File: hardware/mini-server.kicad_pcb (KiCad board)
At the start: 6 copper layers, 1 part, among them U1 NT5CB256M16ER-FL

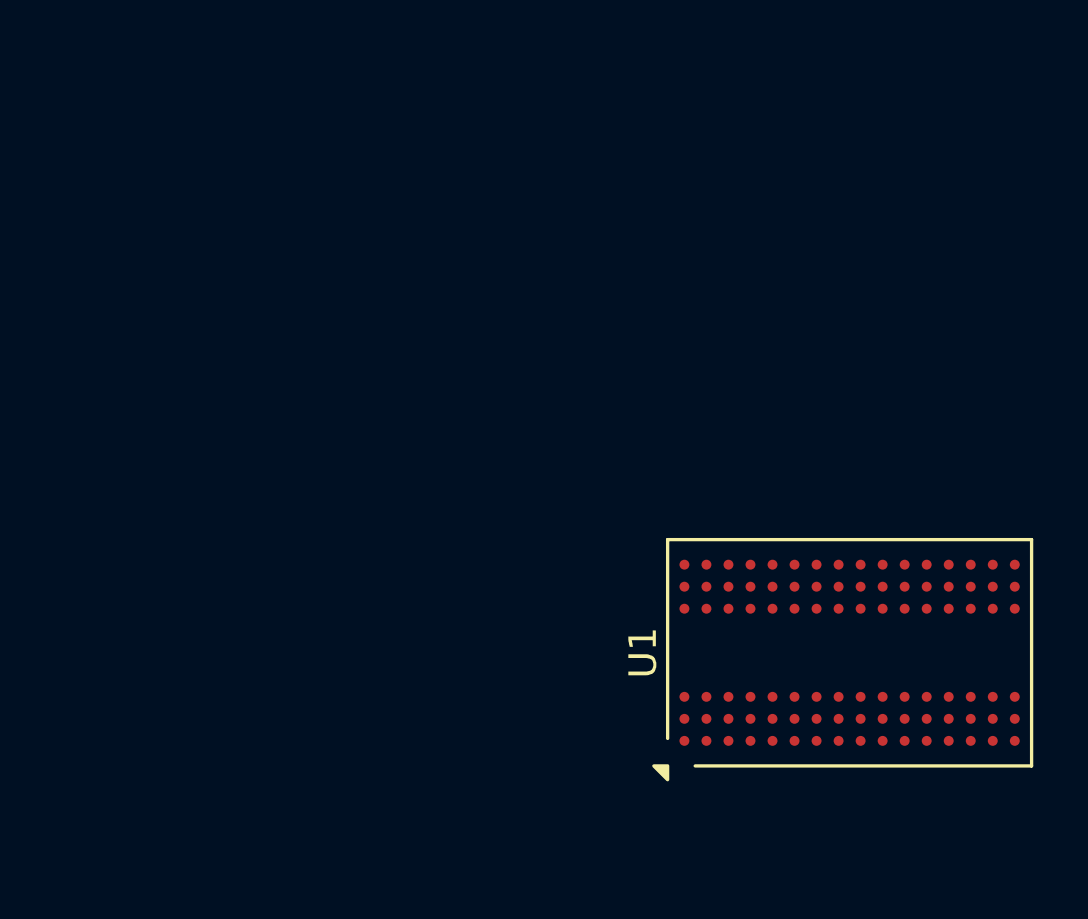
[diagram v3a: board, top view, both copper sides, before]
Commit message: Address and Control signals of DDR3 ram routed
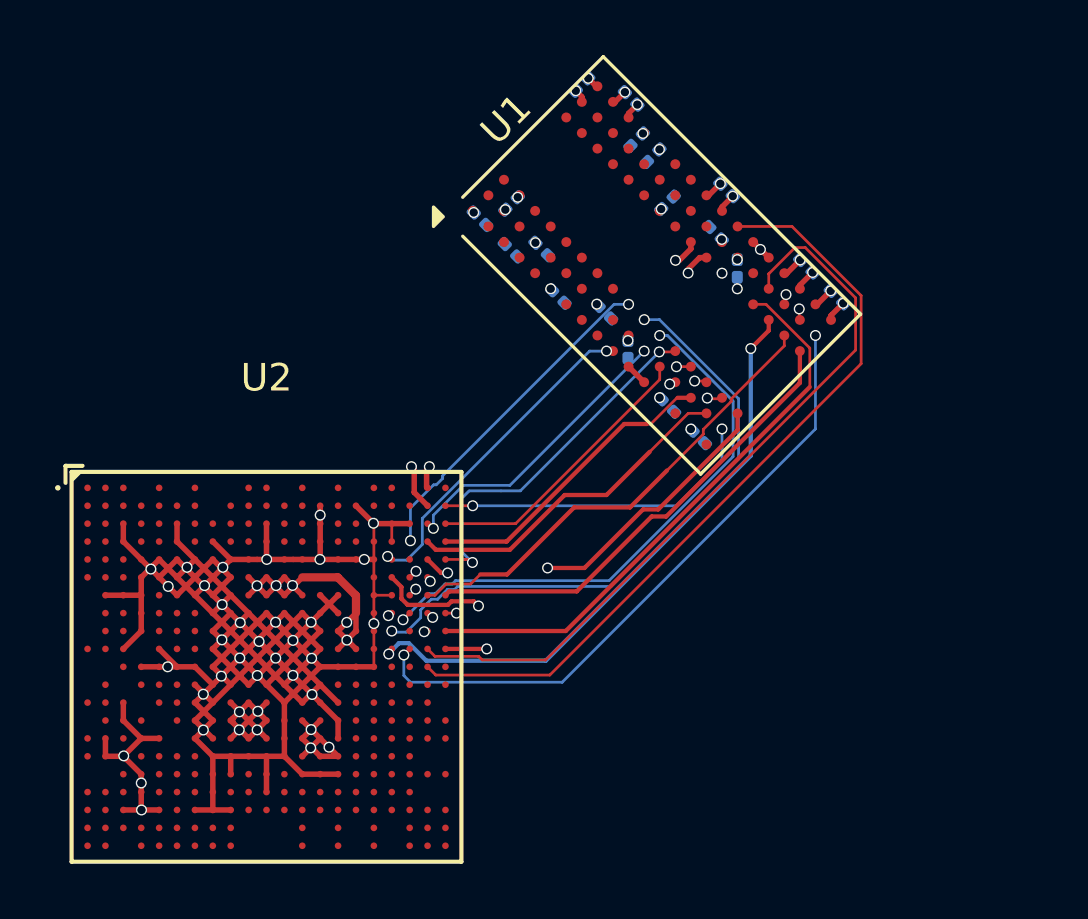
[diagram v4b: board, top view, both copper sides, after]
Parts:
- added C0: 100n, Capacitor_SMD:C_0201_0603Metric, B.Cu at (138.5, 74.4)
- added C1: 100n, Capacitor_SMD:C_0201_0603Metric, B.Cu at (137.4, 75.0)
- added C10: 100n, Capacitor_SMD:C_0201_0603Metric, B.Cu at (142.8, 70.6)
- added C11: 100n, Capacitor_SMD:C_0201_0603Metric, B.Cu at (143.0, 72.1)
- added C12: 100n, Capacitor_SMD:C_0201_0603Metric, B.Cu at (143.6, 72.7)
- added C13: 100n, Capacitor_SMD:C_0201_0603Metric, B.Cu at (146.3, 73.9)
- added C14: 100n, Capacitor_SMD:C_0201_0603Metric, B.Cu at (144.2, 74.4)
- added C15: 100n, Capacitor_SMD:C_0201_0603Metric, B.Cu at (145.9, 75.5)
- added C16: 100n, Capacitor_SMD:C_0201_0603Metric, B.Cu at (149.2, 76.7)
- added C17: 100n, Capacitor_SMD:C_0201_0603Metric, B.Cu at (150.3, 77.8)
- added C2: 100n, Capacitor_SMD:C_0201_0603Metric, B.Cu at (138.5, 76.1)
- added C3: 100n, Capacitor_SMD:C_0201_0603Metric, B.Cu at (140.2, 77.8)
- added C4: 100n, Capacitor_SMD:C_0201_0603Metric, B.Cu at (141.9, 78.4)
- added C5: 100n, Capacitor_SMD:C_0201_0603Metric, B.Cu at (142.7, 79.7)
- added C6: 100n, Capacitor_SMD:C_0201_0603Metric, B.Cu at (144.2, 81.8)
- added C7: 100n, Capacitor_SMD:C_0201_0603Metric, B.Cu at (145.3, 82.9)
- added C8: 100n, Capacitor_SMD:C_0201_0603Metric, B.Cu at (139.6, 76.1)
- added C9: 100n, Capacitor_SMD:C_0201_0603Metric, B.Cu at (141.1, 70.1)
- added R1: 240, Resistor_SMD:R_0201_0603Metric, B.Cu at (146.7, 76.8)
- added U2: RK3328, easyeda2kicad:TFBGA395_L14.0-W14.0_RK3328, F.Cu at (129.6, 91.2)
- moved U1 15.8 mm to (143.6, 76.7), turned to 45 degrees
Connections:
- U1 pad A1: unconnected-(U1-VDDQ-PadA1) -> +1V5
- U1 pad A2: unconnected-(U1-DQU5-PadA2) -> /DDR3/DQU5
- U1 pad A3: unconnected-(U1-DQU7-PadA3) -> /DDR3/DQU7
- U1 pad A7: unconnected-(U1-DQU4-PadA7) -> /DDR3/DQU4
- U1 pad A8: unconnected-(U1-VDDQ-PadA8) -> +1V5
- U1 pad A9: unconnected-(U1-VSS-PadA9) -> GND
- U1 pad B1: unconnected-(U1-VSSQ-PadB1) -> GND
- U1 pad B2: unconnected-(U1-VDD-PadB2) -> +1V5
- U1 pad B3: unconnected-(U1-VSS-PadB3) -> GND
- U1 pad B7: unconnected-(U1-~{DQSU}-PadB7) -> /DDR3/DQSUN
- U1 pad B8: unconnected-(U1-DQU6-PadB8) -> /DDR3/DQU6
- U1 pad B9: unconnected-(U1-VSSQ-PadB9) -> GND
- U1 pad C1: unconnected-(U1-VDDQ-PadC1) -> +1V5
- U1 pad C2: unconnected-(U1-DQU3-PadC2) -> /DDR3/DQU3
- U1 pad C3: unconnected-(U1-DQU1-PadC3) -> /DDR3/DQU1
- U1 pad C7: unconnected-(U1-DQSU-PadC7) -> /DDR3/DQSUP
- U1 pad C8: unconnected-(U1-DQU2-PadC8) -> /DDR3/DQU2
- U1 pad C9: unconnected-(U1-VDDQ-PadC9) -> +1V5
- U1 pad D1: unconnected-(U1-VSSQ-PadD1) -> GND
- U1 pad D2: unconnected-(U1-VDDQ-PadD2) -> +1V5
- U1 pad D3: unconnected-(U1-DMU-PadD3) -> /DDR3/DMU
- U1 pad D7: unconnected-(U1-DQU0-PadD7) -> /DDR3/DQU0
- U1 pad D8: unconnected-(U1-VSSQ-PadD8) -> GND
- U1 pad D9: unconnected-(U1-VDD-PadD9) -> +1V5
- U1 pad E1: unconnected-(U1-VSS-PadE1) -> GND
- U1 pad E2: unconnected-(U1-VSSQ-PadE2) -> GND
- U1 pad E3: unconnected-(U1-DQL0-PadE3) -> /DDR3/DQL0
- U1 pad E7: unconnected-(U1-DML-PadE7) -> /DDR3/DML
- U1 pad E8: unconnected-(U1-VSSQ-PadE8) -> GND
- U1 pad E9: unconnected-(U1-VDDQ-PadE9) -> +1V5
- U1 pad F1: unconnected-(U1-VDDQ-PadF1) -> +1V5
- U1 pad F2: unconnected-(U1-DQL2-PadF2) -> /DDR3/DQL2
- U1 pad F3: unconnected-(U1-DQSL-PadF3) -> /DDR3/DQSLP
- U1 pad F7: unconnected-(U1-DQL1-PadF7) -> /DDR3/DQL1
- U1 pad F8: unconnected-(U1-DQL3-PadF8) -> /DDR3/DQL3
- U1 pad F9: unconnected-(U1-VSSQ-PadF9) -> GND
- U1 pad G1: unconnected-(U1-VSSQ-PadG1) -> GND
- U1 pad G2: unconnected-(U1-DQL6-PadG2) -> /DDR3/DQL6
- U1 pad G3: unconnected-(U1-~{DQSL}-PadG3) -> /DDR3/DQSLN
- U1 pad G7: unconnected-(U1-VDD-PadG7) -> +1V5
- U1 pad G8: unconnected-(U1-VSS-PadG8) -> GND
- U1 pad G9: unconnected-(U1-VSSQ-PadG9) -> GND
- U1 pad H2: unconnected-(U1-VDDQ-PadH2) -> +1V5
- U1 pad H3: unconnected-(U1-DQL4-PadH3) -> /DDR3/DQL4
- U1 pad H7: unconnected-(U1-DQL7-PadH7) -> /DDR3/DQL7
- U1 pad H8: unconnected-(U1-DQL5-PadH8) -> /DDR3/DQL5
- U1 pad H9: unconnected-(U1-VDDQ-PadH9) -> +1V5
- U1 pad J1: unconnected-(U1-NC-PadJ1) -> GND
- U1 pad J2: unconnected-(U1-VSS-PadJ2) -> GND
- U1 pad J3: unconnected-(U1-~{RAS}-PadJ3) -> /DDR3/RASn
- U1 pad J7: unconnected-(U1-CK-PadJ7) -> /DDR3/CKP
- U1 pad J8: unconnected-(U1-VSS-PadJ8) -> GND
- U1 pad J9: unconnected-(U1-NC-PadJ9) -> GND
- U1 pad K1: unconnected-(U1-ODT-PadK1) -> /DDR3/ODT
- U1 pad K2: unconnected-(U1-VDD-PadK2) -> +1V5
- U1 pad K3: unconnected-(U1-~{CAS_}-PadK3) -> /DDR3/CASn
- U1 pad K7: unconnected-(U1-~{CK}-PadK7) -> /DDR3/CKN
- U1 pad K8: unconnected-(U1-VDD-PadK8) -> +1V5
- U1 pad K9: unconnected-(U1-CKE-PadK9) -> /DDR3/CKE
- U1 pad L1: unconnected-(U1-NC-PadL1) -> GND
- U1 pad L2: unconnected-(U1-~{CS}-PadL2) -> /DDR3/CSn
- U1 pad L3: unconnected-(U1-~{WE}-PadL3) -> /DDR3/WEn
- U1 pad L7: unconnected-(U1-A10/AP-PadL7) -> /DDR3/A10
- U1 pad L8: unconnected-(U1-ZQ-PadL8) -> Net-(U1-ZQ)
- U1 pad L9: unconnected-(U1-NC-PadL9) -> GND
- U1 pad M1: unconnected-(U1-VSS-PadM1) -> GND
- U1 pad M2: unconnected-(U1-BA0-PadM2) -> /DDR3/BA0
- U1 pad M3: unconnected-(U1-BA2-PadM3) -> /DDR3/BA2
- U1 pad M7: unconnected-(U1-NC-PadM7) -> GND
- U1 pad M9: unconnected-(U1-VSS-PadM9) -> GND
- U1 pad N1: unconnected-(U1-VDD-PadN1) -> +1V5
- U1 pad N2: unconnected-(U1-A3-PadN2) -> /DDR3/A3
- U1 pad N3: unconnected-(U1-A0-PadN3) -> /DDR3/A0
- U1 pad N7: unconnected-(U1-A12/~{BC}-PadN7) -> /DDR3/A12
- U1 pad N8: unconnected-(U1-BA1-PadN8) -> /DDR3/BA1
- U1 pad N9: unconnected-(U1-VDD-PadN9) -> +1V5
- U1 pad P1: unconnected-(U1-VSS-PadP1) -> GND
- U1 pad P2: unconnected-(U1-A5-PadP2) -> /DDR3/A5
- U1 pad P3: unconnected-(U1-A2-PadP3) -> /DDR3/A2
- U1 pad P7: unconnected-(U1-A1-PadP7) -> /DDR3/A1
- U1 pad P8: unconnected-(U1-A4-PadP8) -> /DDR3/A4
- U1 pad P9: unconnected-(U1-VSS-PadP9) -> GND
- U1 pad R1: unconnected-(U1-VDD-PadR1) -> +1V5
- U1 pad R2: unconnected-(U1-A7-PadR2) -> /DDR3/A7
- U1 pad R3: unconnected-(U1-A9-PadR3) -> /DDR3/A9
- U1 pad R7: unconnected-(U1-A11-PadR7) -> /DDR3/A11
- U1 pad R8: unconnected-(U1-A6-PadR8) -> /DDR3/A6
- U1 pad R9: unconnected-(U1-VDD-PadR9) -> +1V5
- U1 pad T1: unconnected-(U1-VSS-PadT1) -> GND
- U1 pad T2: unconnected-(U1-~{RESET}-PadT2) -> /DDR3/RSTn
- U1 pad T3: unconnected-(U1-A13-PadT3) -> /DDR3/A13
- U1 pad T7: unconnected-(U1-A14-PadT7) -> /DDR3/A14
- U1 pad T8: unconnected-(U1-A8-PadT8) -> /DDR3/A8
- U1 pad T9: unconnected-(U1-VSS-PadT9) -> GND
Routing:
- net GND: track 0.00 -> 136.9 mm, vias 0 -> 41
- net /DDR3/CKE: track 0.00 -> 28.6 mm
- net /DDR3/BA1: track 0.00 -> 27.2 mm
- net /DDR3/A10: track 0.00 -> 26.5 mm, vias 0 -> 2
- net /DDR3/A8: track 0.00 -> 23.3 mm, vias 0 -> 2
- net /DDR3/CASn: track 0.00 -> 22.2 mm, vias 0 -> 2
- net /DDR3/A1: track 0.00 -> 22.1 mm, vias 0 -> 2
- net /DDR3/A12: track 0.00 -> 21.0 mm
- net /DDR3/WEn: track 0.00 -> 20.5 mm, vias 0 -> 2
- net /DDR3/A6: track 0.00 -> 20.2 mm, vias 0 -> 2
- net /DDR3/A4: track 0.00 -> 19.4 mm, vias 0 -> 2
- net /DDR3/A2: track 0.00 -> 17.4 mm, vias 0 -> 2
- net /DDR3/A11: track 0.00 -> 17.2 mm
- net /DDR3/A14: track 0.00 -> 17.2 mm
- net /DDR3/A13: track 0.00 -> 16.6 mm, vias 0 -> 2
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
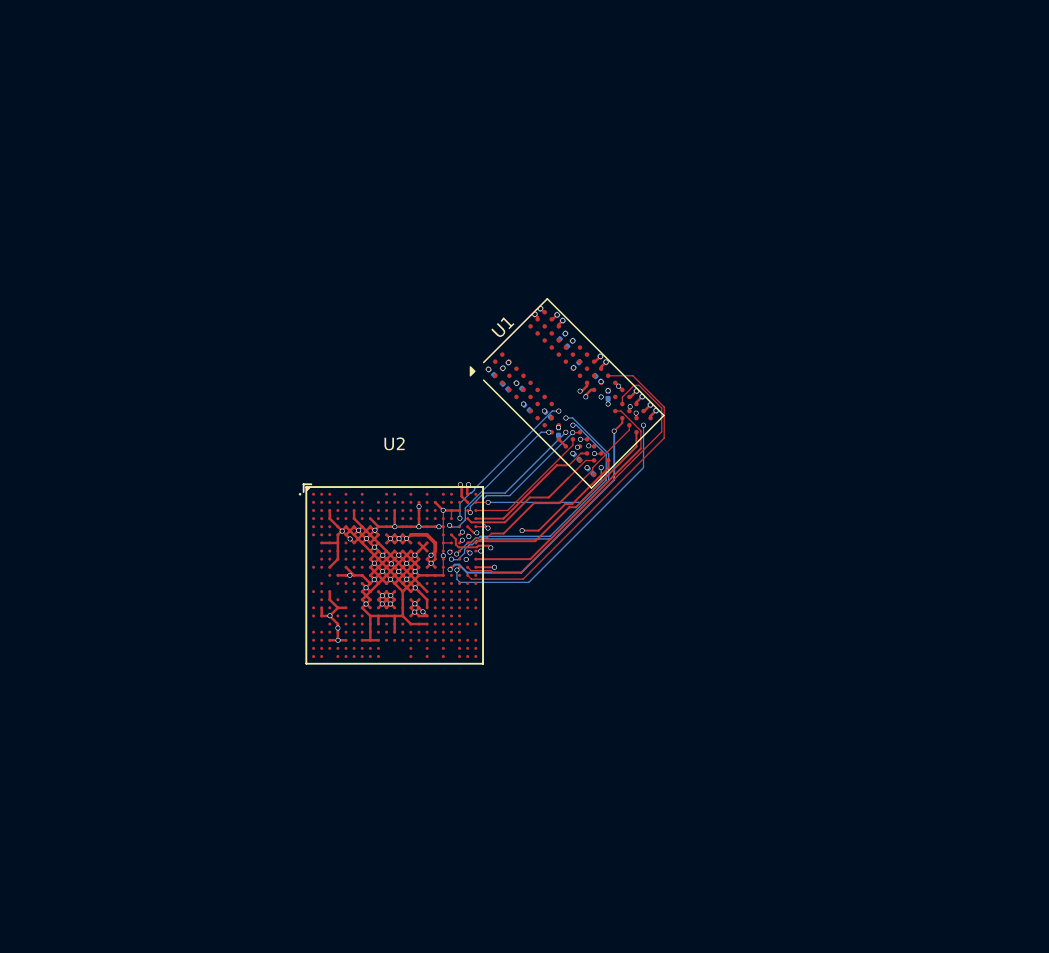
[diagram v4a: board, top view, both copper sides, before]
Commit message: DQ lines routed from the RK3328 to DDR3 RAM
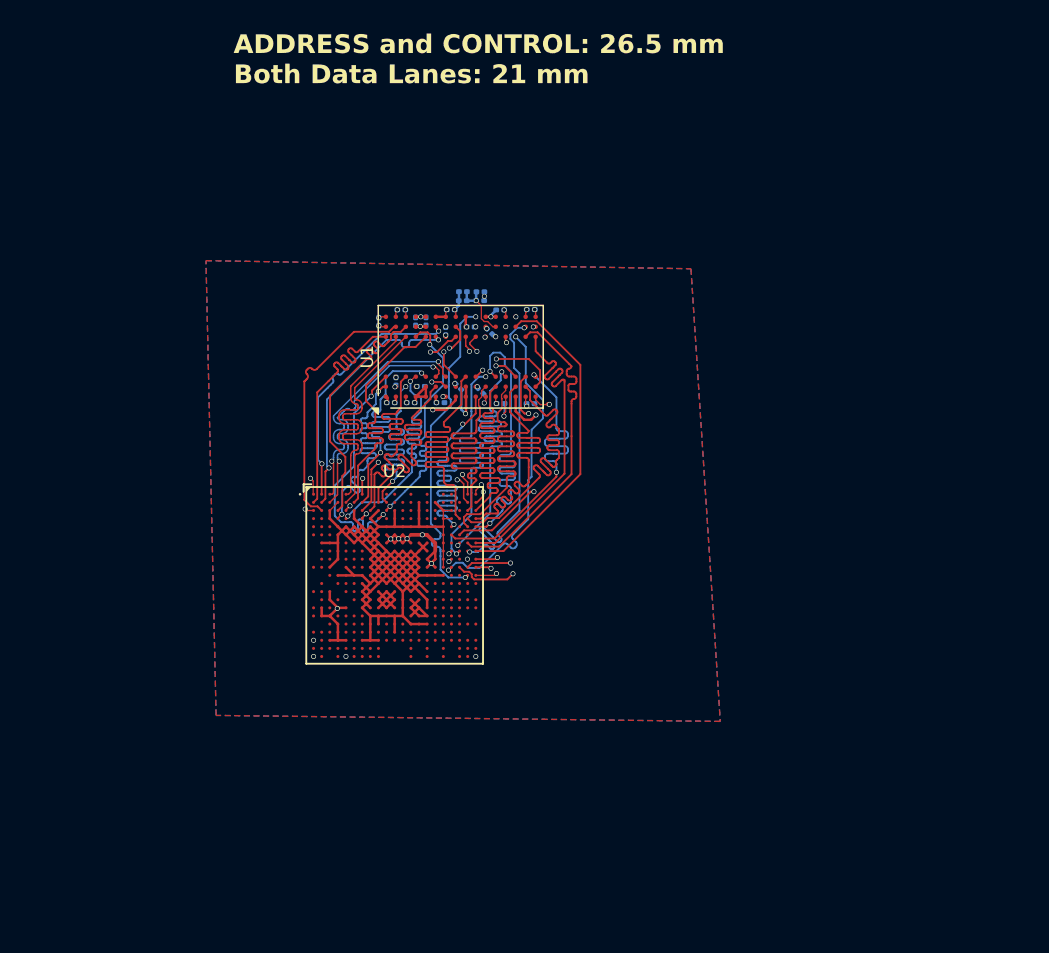
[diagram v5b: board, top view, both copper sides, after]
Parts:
- added C18: 100n, Capacitor_SMD:C_0201_0603Metric, B.Cu at (135.1, 68.5)
- added C19: 100n, Capacitor_SMD:C_0201_0603Metric, B.Cu at (136.5, 68.5)
- added R2: 10k, Resistor_SMD:R_0201_0603Metric, B.Cu at (135.1, 69.2)
- added R3: 10k, Resistor_SMD:R_0201_0603Metric, B.Cu at (136.4, 69.2)
- moved C7 20.8 mm to (128.3, 70.9), turned to 90 degrees
- moved C16 20.2 mm to (130.1, 70.0), turned to 180 degrees
- moved C17 18.0 mm to (134.1, 70.0), turned to 180 degrees
- moved C15 14.5 mm to (132.1, 70.9), turned to -90 degrees
- moved C14 13.3 mm to (131.3, 70.9), turned to -90 degrees
- moved R1 10.8 mm to (137.2, 71.7), turned to -45 degrees
- moved C0 9.69 mm to (129.3, 77.4), turned to 0 degrees
- moved C6 9.34 mm to (136.5, 76.5)
- moved U1 9.19 mm to (134.9, 73.7), turned to 90 degrees
- moved C13 8.96 mm to (138.1, 77.5), turned to 180 degrees
- moved C5 8.80 mm to (134.7, 76.1), turned to -45 degrees
- moved C4 8.68 mm to (133.3, 77.4), turned to 0 degrees
- moved C3 8.67 mm to (131.7, 76.1), turned to 0 degrees
- moved C2 7.70 mm to (130.9, 77.4), turned to 0 degrees
- moved C1 7.68 mm to (129.7, 75.7), turned to 90 degrees
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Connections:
- U1 pad A2: /DDR3/DQU5 -> /DDR3/DQU4
- U1 pad A7: /DDR3/DQU4 -> /DDR3/DQU0
- U1 pad B8: /DDR3/DQU6 -> /DDR3/DQU2
- U1 pad C8: /DDR3/DQU2 -> /DDR3/DQU6
- U1 pad D7: /DDR3/DQU0 -> /DDR3/DQU5
- U1 pad E3: /DDR3/DQL0 -> /DDR3/DQL6
- U1 pad F2: /DDR3/DQL2 -> /DDR3/DQL4
- U1 pad F7: /DDR3/DQL1 -> /DDR3/DQL3
- U1 pad F8: /DDR3/DQL3 -> /DDR3/DQL7
- U1 pad G2: /DDR3/DQL6 -> /DDR3/DQL0
- U1 pad H1: unconnected-(U1-VREFDQ-PadH1) -> Net-(U1-VREFCA)
- U1 pad H3: /DDR3/DQL4 -> /DDR3/DQL5
- U1 pad H7: /DDR3/DQL7 -> /DDR3/DQL2
- U1 pad H8: /DDR3/DQL5 -> /DDR3/DQL1
- U1 pad M8: unconnected-(U1-VREFCA-PadM8) -> Net-(U1-VREFCA)
- U2 pad A3: unconnected-(U2C-DDR_DQS0_N-PadA3) -> /DDR3/DQSLN
- U2 pad A5: unconnected-(U2C-DDR_DQS1_N-PadA5) -> /DDR3/DQSUN
- U2 pad B3: unconnected-(U2C-DDR_DQS0_P-PadB3) -> /DDR3/DQSLP
- U2 pad B5: unconnected-(U2C-DDR_DQS1_P-PadB5) -> /DDR3/DQSUP
- U2 pad B6: unconnected-(U2C-DDR_DM0-PadB6) -> /DDR3/DML
- U2 pad D5: unconnected-(U2C-DDR_DM1-PadD5) -> /DDR3/DMU
- U2 pad F10: Net-(U2B-VDD_DDRIO_1) -> +1V5
- U2 pad F11: Net-(U2B-VDD_DDRIO_1) -> +1V5
- U2 pad F12: Net-(U2B-VDD_DDRIO_1) -> +1V5
- U2 pad F13: Net-(U2B-VDD_DDRIO_1) -> +1V5
- U2 pad G10: Net-(U2B-VDD_DDRIO_1) -> +1V5
- U2 pad G11: Net-(U2B-VDD_DDRIO_1) -> +1V5
- U2 pad G12: Net-(U2B-VDD_DDRIO_1) -> +1V5
- U2 pad G13: Net-(U2B-VDD_DDRIO_1) -> +1V5
- U2 pad H16: Net-(U2B-VDD_DDRIO_1) -> +1V5
- U2 pad J15: Net-(U2B-VDD_DDRIO_1) -> +1V5
- U2 pad J16: Net-(U2B-VDD_DDRIO_1) -> +1V5
- U2 pad K15: Net-(U2B-VDD_DDRIO_1) -> +1V5
- U2 pad K16: Net-(U2B-VDD_DDRIO_1) -> +1V5
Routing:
- net GND: track 136.9 -> 157.9 mm, vias 41 -> 30
- net /DDR3/DQU2: track 0.00 -> 21.0 mm
- net /DDR3/DQU6: track 0.00 -> 20.9 mm
- net /DDR3/DML: track 0.00 -> 20.9 mm
- net /DDR3/DQU0: track 0.00 -> 20.9 mm
- net /DDR3/DQL4: track 0.00 -> 20.9 mm
- net /DDR3/DQSUP: track 0.00 -> 20.9 mm
- net /DDR3/DQU1: track 0.00 -> 20.8 mm
- net /DDR3/DQL2: track 0.00 -> 20.8 mm, vias 0 -> 2
- net /DDR3/DQL1: track 0.00 -> 20.8 mm, vias 0 -> 2
- net /DDR3/DQL0: track 0.00 -> 20.8 mm, vias 0 -> 2
- net /DDR3/DQL5: track 0.00 -> 20.8 mm, vias 0 -> 2
- net /DDR3/DQSLP: track 0.00 -> 20.6 mm, vias 0 -> 2
- net /DDR3/DQL7: track 0.00 -> 20.6 mm, vias 0 -> 2
- net /DDR3/DQL3: track 0.00 -> 20.6 mm, vias 0 -> 2
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- added copper zone on In3.Cu, net +1V5
- added copper zone on B.Cu, net GND
- added copper zone on F.Cu, net GND
- added copper zone on In1.Cu, net GND
- added copper zone on In2.Cu, net GND
- added copper zone on In4.Cu, net GND
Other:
- board text added: "ADDRESS and CONTROL: 26.5 mm Both Data Lanes: 21 mm"
